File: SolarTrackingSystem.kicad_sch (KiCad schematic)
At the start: 8 parts, among them J1 Servo Pin Connector, J2 LDR Terminal, J3 LDR Terminal (1)

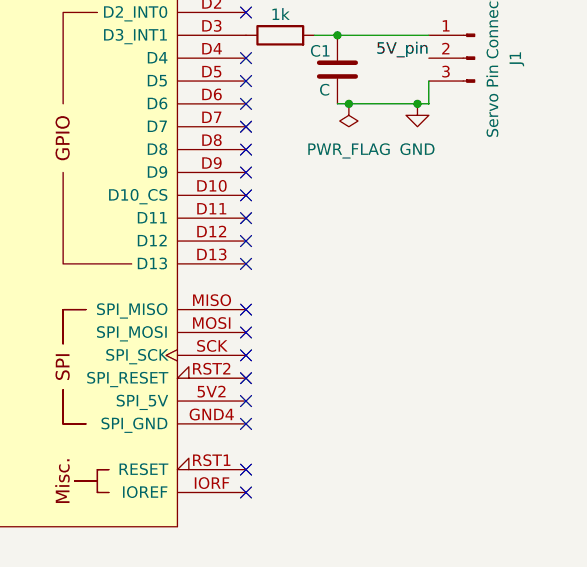
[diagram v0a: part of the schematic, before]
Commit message: added LED Debug Indicator
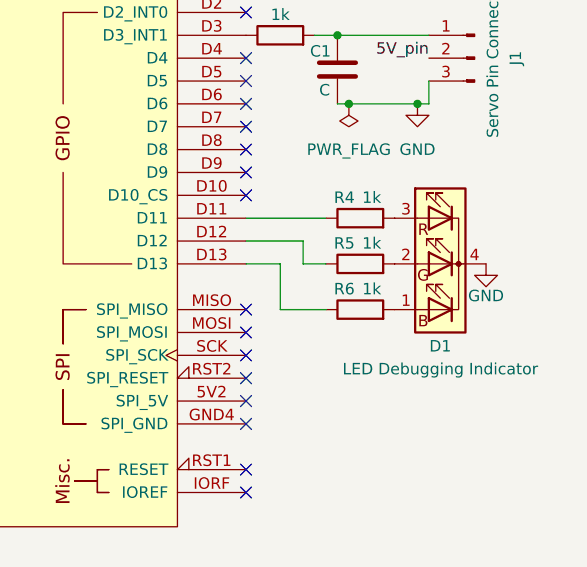
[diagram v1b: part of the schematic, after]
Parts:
- added D1: LED Debugging Indicator, LED_THT:LED_D5.0mm-4_RGB, symbol Device:LED_BGRK
- added R4, R5, R6: 1k, Resistor_THT:R_Axial_DIN0411_L9.9mm_D3.6mm_P12.70mm_Horizontal, symbol Device:R
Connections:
- net GND: now also D1.4 (K)
- net at A1.D11: now also R4.1
- net at A1.D12: now also R5.1
- net at A1.D13: now also R6.1
- new net: D1.1 (BA), R6.2
- new net: D1.2 (GA), R5.2
- new net: D1.3 (RA), R4.2
- no-connect marks 31 -> 28

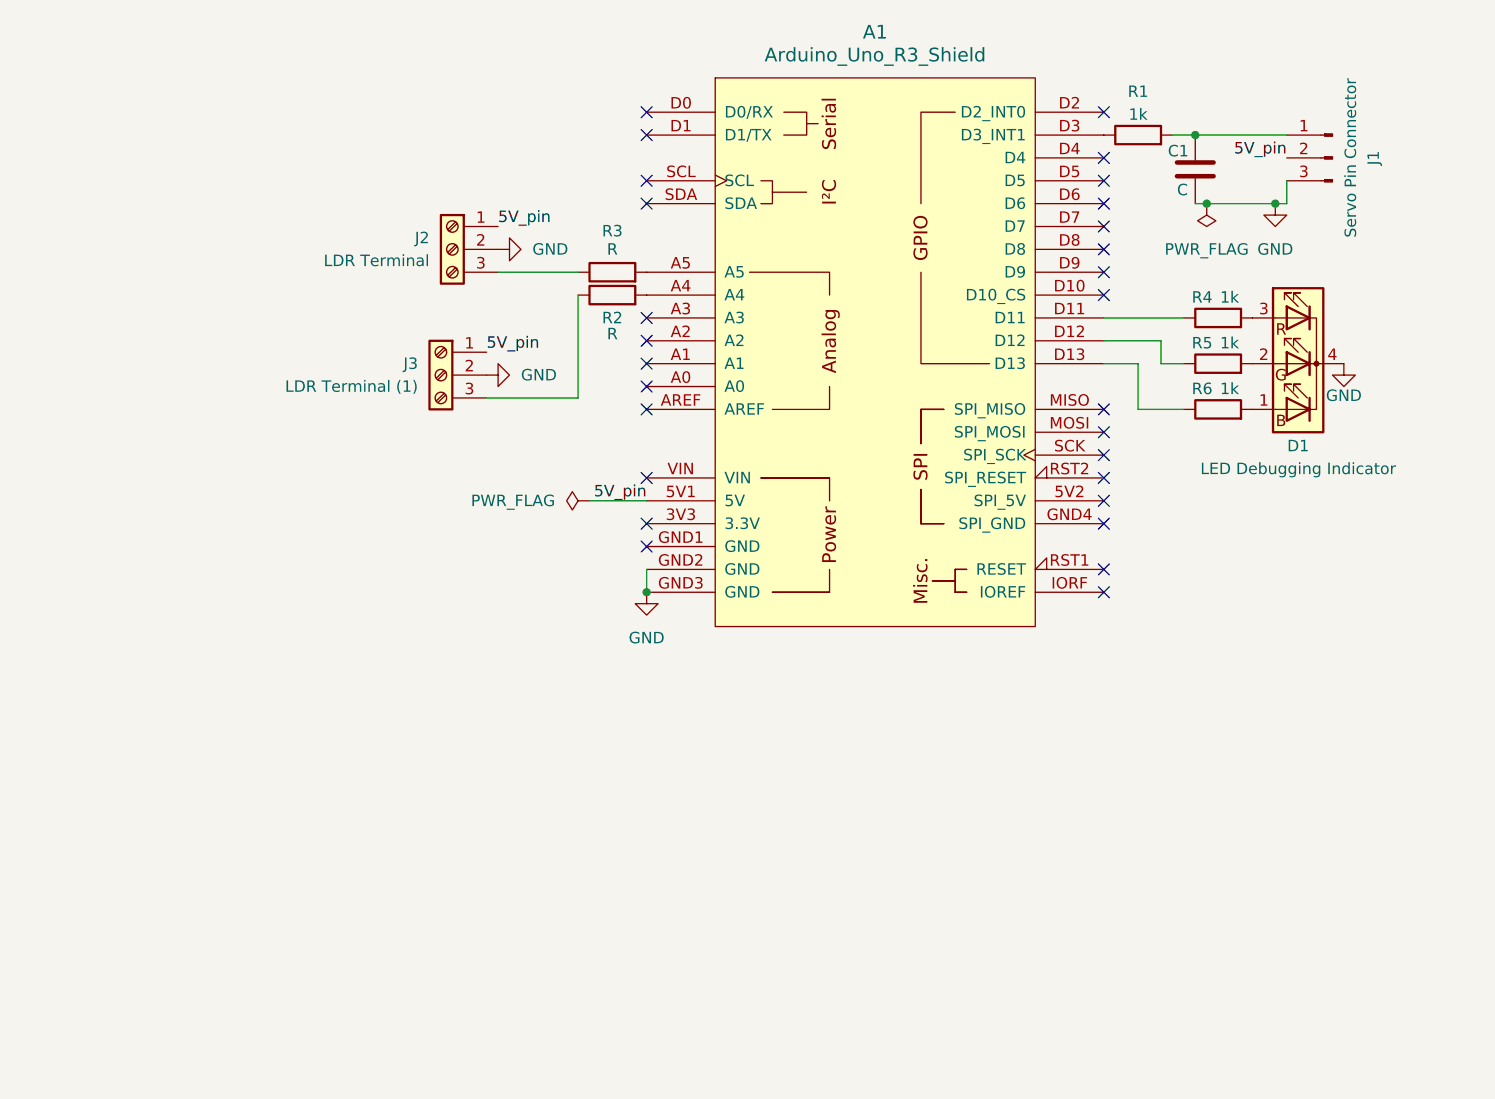
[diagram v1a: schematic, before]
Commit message: new feature
added real-time clock
changed from single sided pcb to double sided
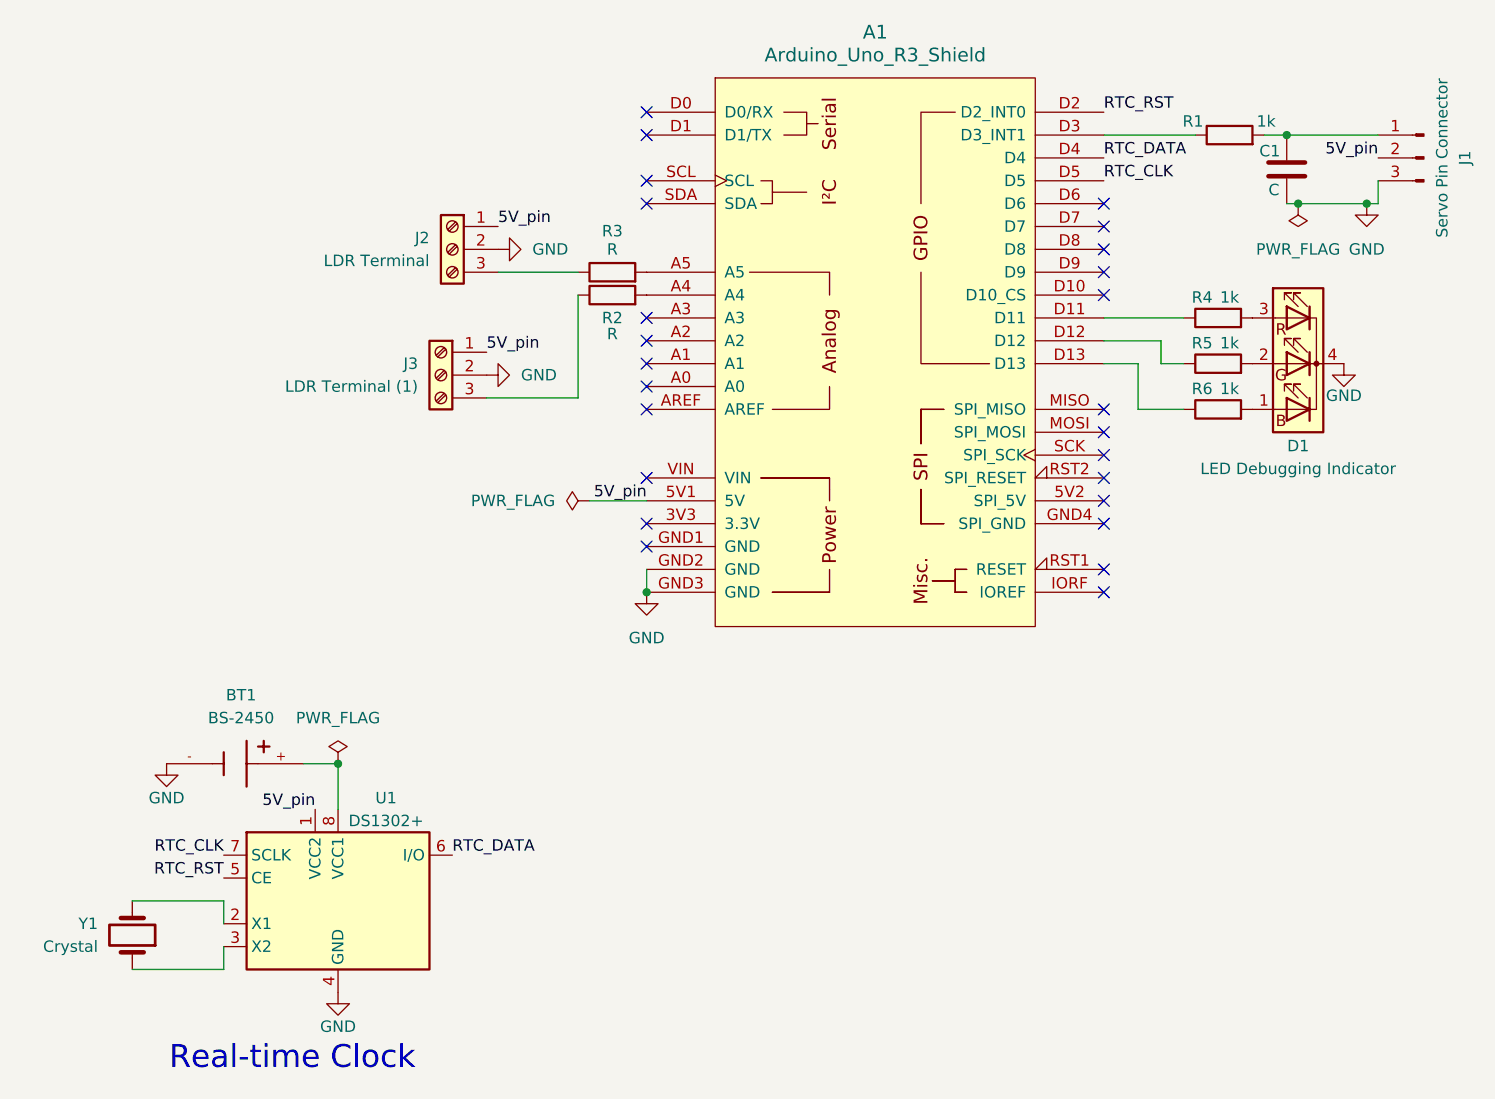
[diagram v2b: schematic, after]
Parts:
- added BT1: BS-2450, BS-2450:BAT_BS-2450, symbol BS-2450:BS-2450
- added U1: DS1302+, Package_DIP:DIP-8_W7.62mm, symbol Timer_RTC:DS1302+
- added Y1: Crystal, Crystal:Crystal_DS10_D1.0mm_L4.3mm_Horizontal, symbol Device:Crystal
- J2, J3: footprint TerminalBlock:TerminalBlock_bornier-3_P5.08mm -> TerminalBlock_Phoenix:TerminalBlock_Phoenix_MKDS-1,5-3_1x03_P5.00mm_Horizontal
- R1, R2, R3, R4, R5, R6: footprint Resistor_THT:R_Axial_DIN0411_L9.9mm_D3.6mm_P12.70mm_Horizontal -> Resistor_THT:R_Axial_DIN0207_L6.3mm_D2.5mm_P7.62mm_Horizontal
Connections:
- net 5V_pin: now also U1.1 (VCC2)
- net GND: now also BT1.-, U1.4 (GND)
- net RTC_RST: now reaches A1.D2 (D2_INT0)
- net RTC_RST: now also U1.5 (CE)
- net RTC_DATA: now reaches A1.D4
- net RTC_DATA: now also U1.6 (I/O)
- net RTC_CLK: now reaches A1.D5
- net RTC_CLK: now also U1.7 (SCLK)
- new net: BT1.+, U1.8 (VCC1)
- new net: U1.2 (X1), Y1.2
- new net: U1.3 (X2), Y1.1
- no-connect marks 28 -> 25
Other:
- note added: "Real-time Clock"
- moved on the sheet: C1, J1, R1
